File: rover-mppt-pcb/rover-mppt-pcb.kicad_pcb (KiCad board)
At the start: 2 copper layers, 59 x 30 mm, 15 parts, among them J1 OC, Q1 SiR880BDP, Q2 SiR880BDP, U1 BQ25820RRVR

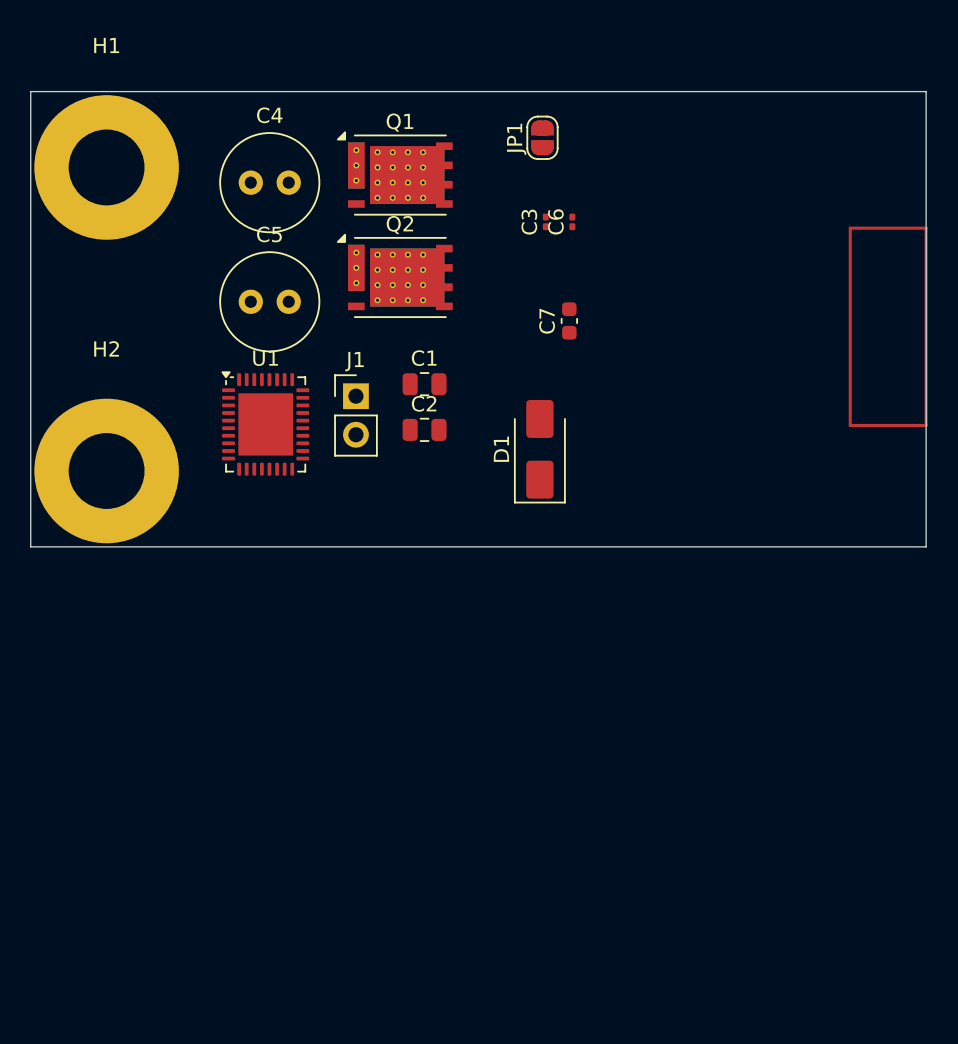
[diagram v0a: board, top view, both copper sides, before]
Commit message: Created thermal DAQ
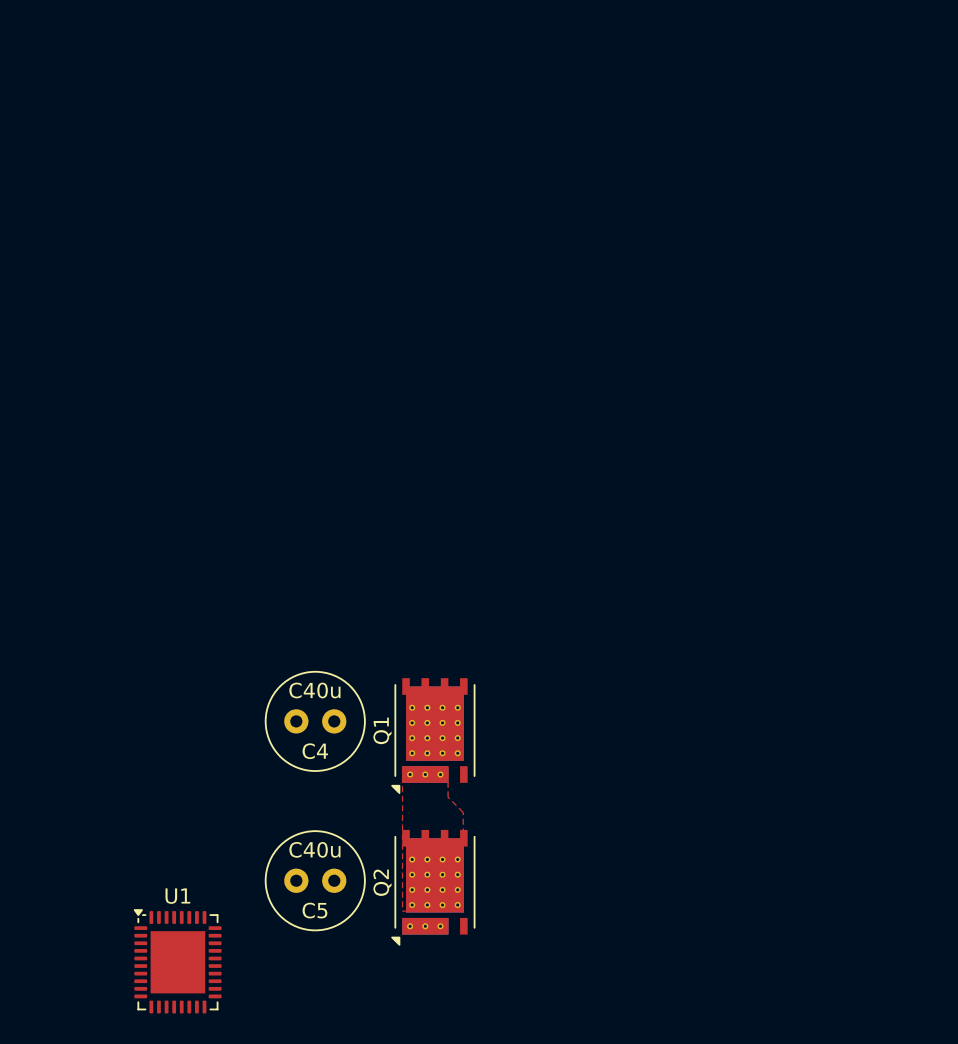
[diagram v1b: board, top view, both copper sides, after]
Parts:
- removed C1: C2u2, Capacitor_SMD:C_0805_2012Metric
- removed C2: C1u, Capacitor_SMD:C_0805_2012Metric
- removed C3, C6: C470n, Capacitor_SMD:C_0201_0603Metric
- removed C7: C47n, Capacitor_SMD:C_0603_1608Metric
- removed D1: SS14-M3/5AT, Diode_SMD:D_SMA
- removed H1, H2: MP, footprints:RING#10_hole
- removed J1: OC, Connector_PinHeader_2.54mm:PinHeader_1x02_P2.54mm_Vertical
- removed JP1: OC, Jumper:SolderJumper-2_P1.3mm_Open_RoundedPad1.0x1.5mm
- moved Q2 39.9 mm to (111.6, 117.1), turned to 90 degrees
- moved C5 38.5 mm to (105.0, 117.0), turned to 180 degrees
- moved Q1 36.7 mm to (111.6, 107.1), turned to 90 degrees
- moved C4 35.9 mm to (105.0, 106.5), turned to 180 degrees
- moved U1 35.9 mm to (94.7, 122.4)
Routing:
- added copper zone on F.Cu, net /VSW
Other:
- board outline removed
